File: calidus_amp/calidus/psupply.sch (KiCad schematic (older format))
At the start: 44 parts, among them U1 L7805, U2 LM317_3PinPackage, U3 LM337_TO220

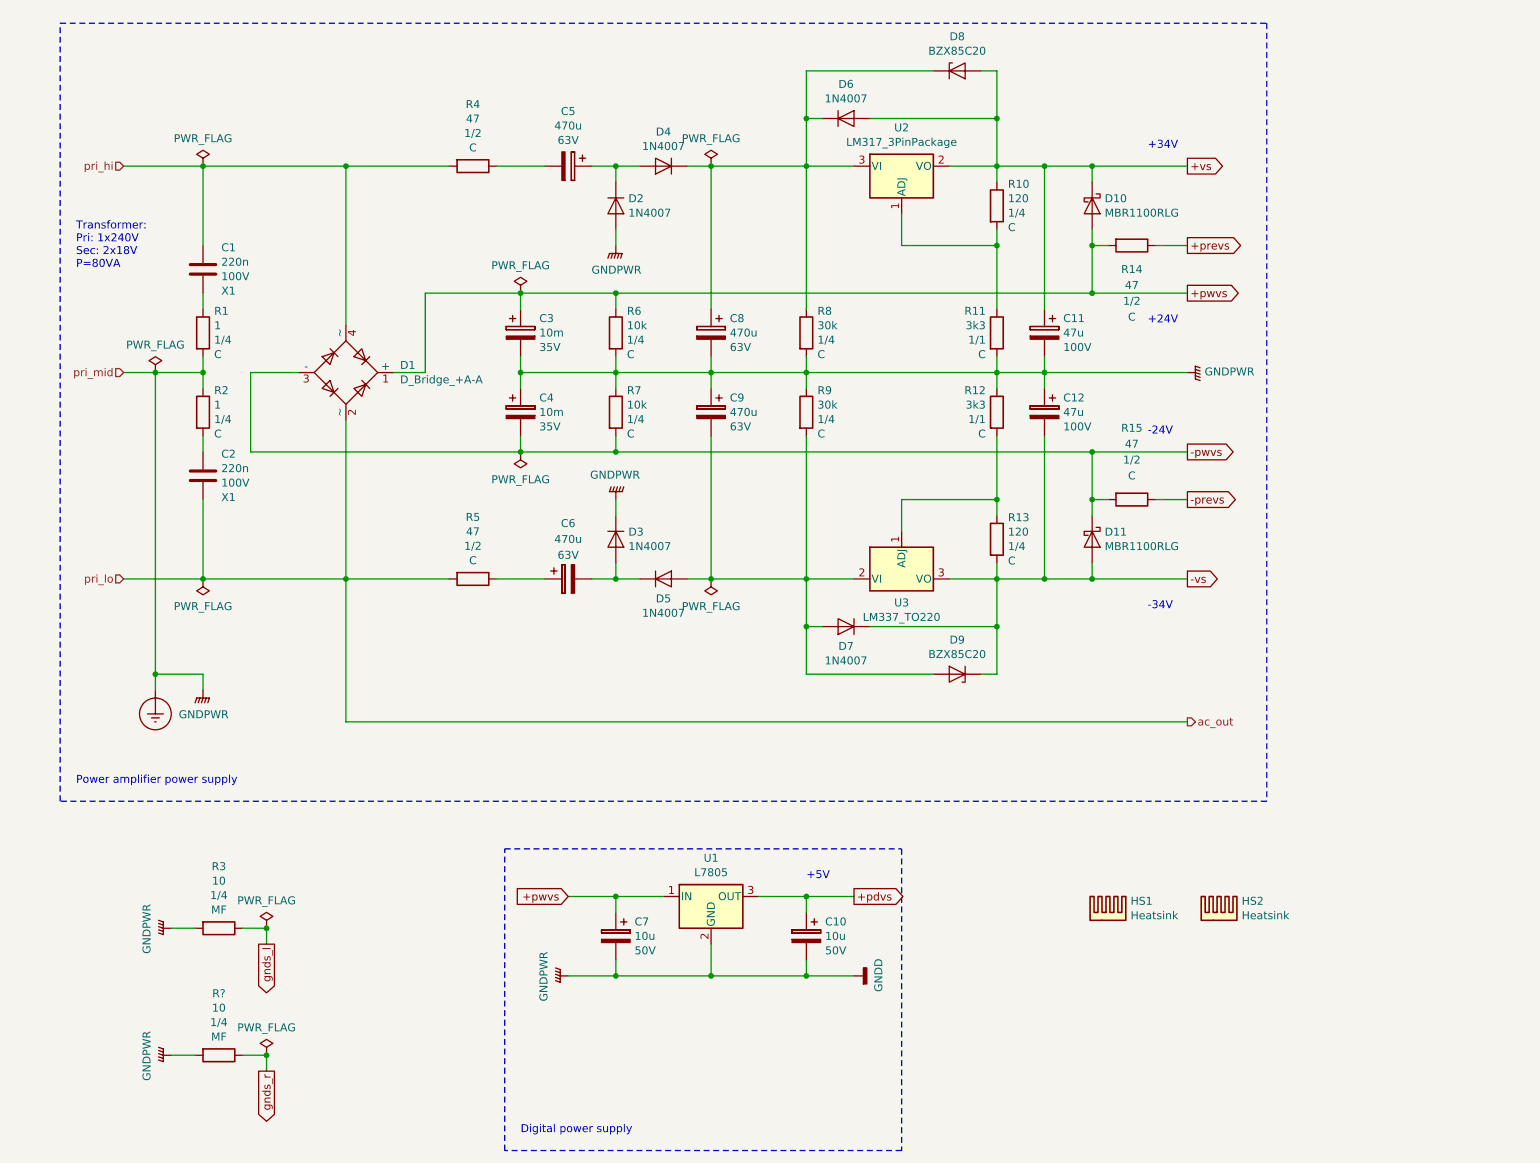
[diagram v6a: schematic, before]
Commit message: WIP: Component placement on PCB
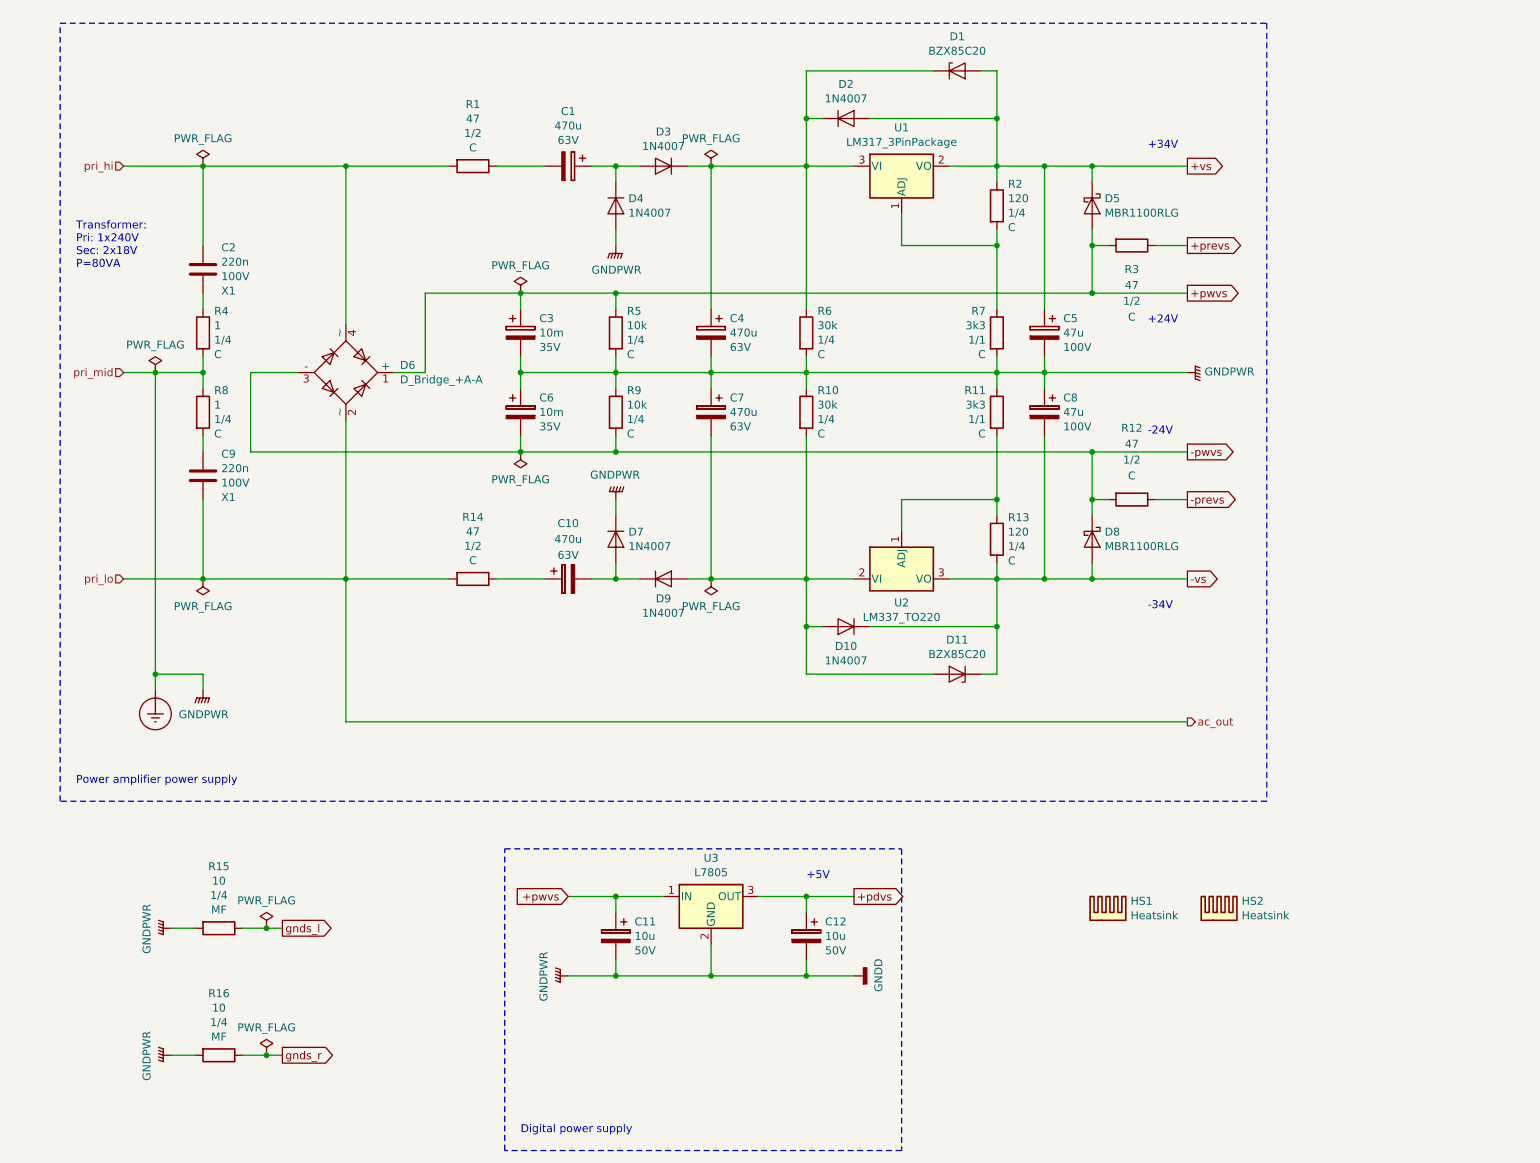
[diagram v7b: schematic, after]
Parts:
- gave numbers to parts that had none: 1
- renumbered C5 to C1, C6 to C10, C7 to C11, C10 to C12, C1 to C2, C8 to C4, C11 to C5, C4 to C6, C9 to C7, C12 to C8, C2 to C9, D8 to D1, D7 to D10, D9 to D11, D6 to D2, D4 to D3, D2 to D4, D10 to D5, D1 to D6, D3 to D7, D11 to D8, D5 to D9, R4 to R1, R9 to R10, R12 to R11, R15 to R12, R5 to R14, R3 to R15, R10 to R2, R14 to R3, R1 to R4, R6 to R5, R8 to R6, R11 to R7, R2 to R8, R7 to R9, U2 to U1, U3 to U2, U1 to U3

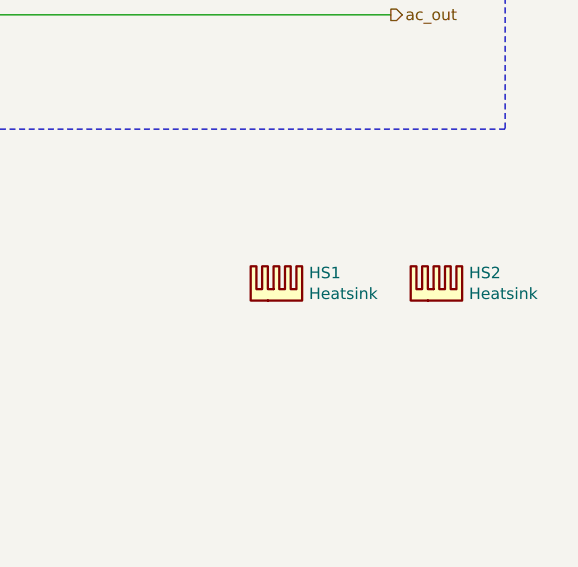
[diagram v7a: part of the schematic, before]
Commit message: WIP: Removed unnecessary heatsinks
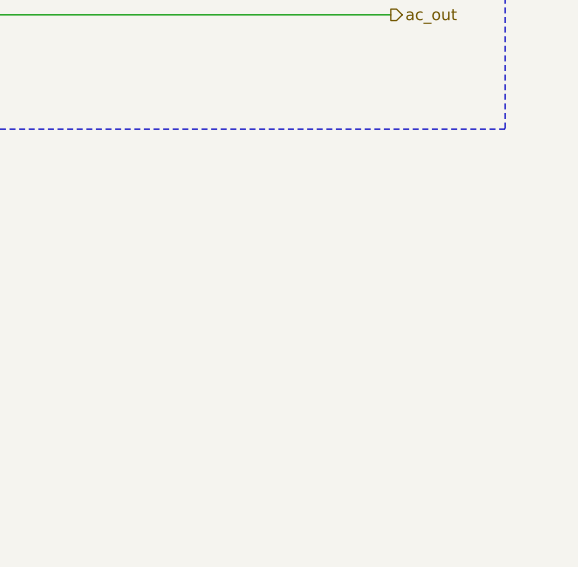
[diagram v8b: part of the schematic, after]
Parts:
- removed HS1, HS2: Heatsink, Heatsink:Heatsink_Fischer_SK104-STCB_35x13mm__2xDrill3.5mm_ScrewM3, symbol Mechanical:Heatsink
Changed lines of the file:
@@
 Power amplifier power supply
-$Comp
-L Mechanical:Heatsink HS1
-U 1 1 5C460FCB
-P 8000 6250
-F 0 "HS1" H 8142 6371 50  0000 L CNN
-F 1 "Heatsink" H 8142 6280 50  0000 L CNN
-F 2 "Heatsink:Heatsink_Fischer_SK104-STCB_35x13mm__2xDrill3.5mm_ScrewM3" H 8012 6250 50  0001 C CNN
-F 3 "" H 8012 6250 50  0001 C CNN
-	1    8000 6250
-	1    0    0    -1
-$EndComp
-$Comp
-L Mechanical:Heatsink HS2
-U 1 1 5C4610C3
-P 8700 6250
-F 0 "HS2" H 8842 6371 50  0000 L CNN
-F 1 "Heatsink" H 8842 6280 50  0000 L CNN
-F 2 "Heatsink:Heatsink_Fischer_SK104-STCB_35x13mm__2xDrill3.5mm_ScrewM3" H 8712 6250 50  0001 C CNN
-F 3 "" H 8712 6250 50  0001 C CNN
-	1    8700 6250
-	1    0    0    -1
-$EndComp
 $Comp
 L Regulator_Linear:LM337_TO220 U2
